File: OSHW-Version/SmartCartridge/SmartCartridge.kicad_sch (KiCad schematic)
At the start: 9 parts

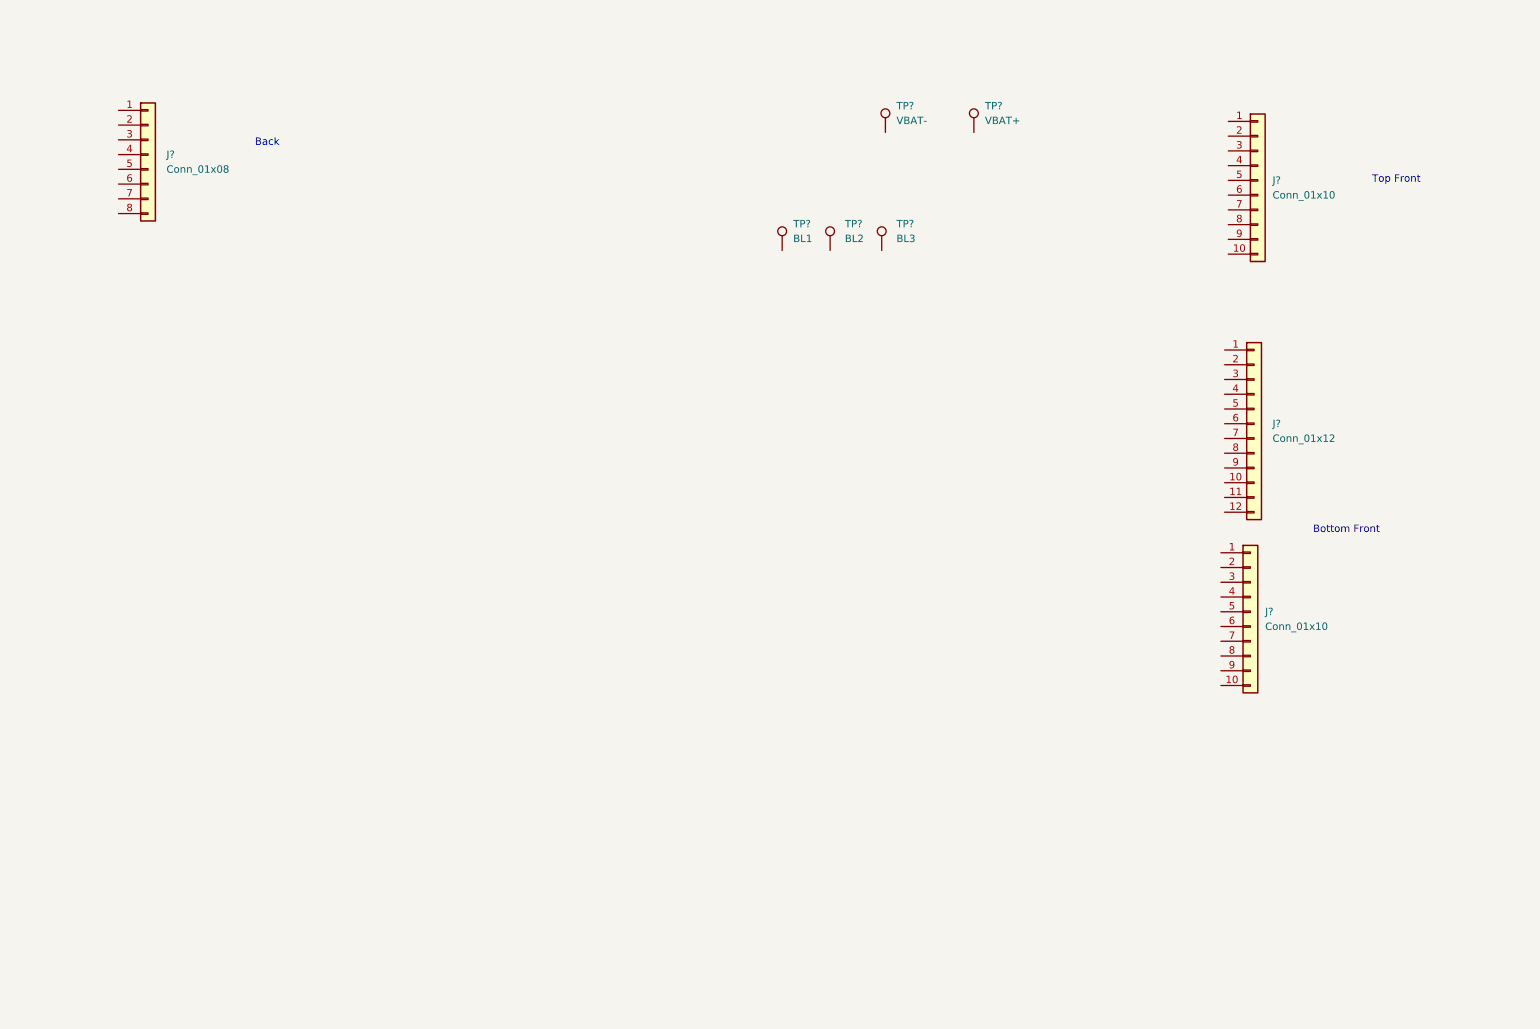
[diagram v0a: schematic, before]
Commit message: SmartCartridge Kicad : brushless, battery connector and button placement
+ spotted all the ground
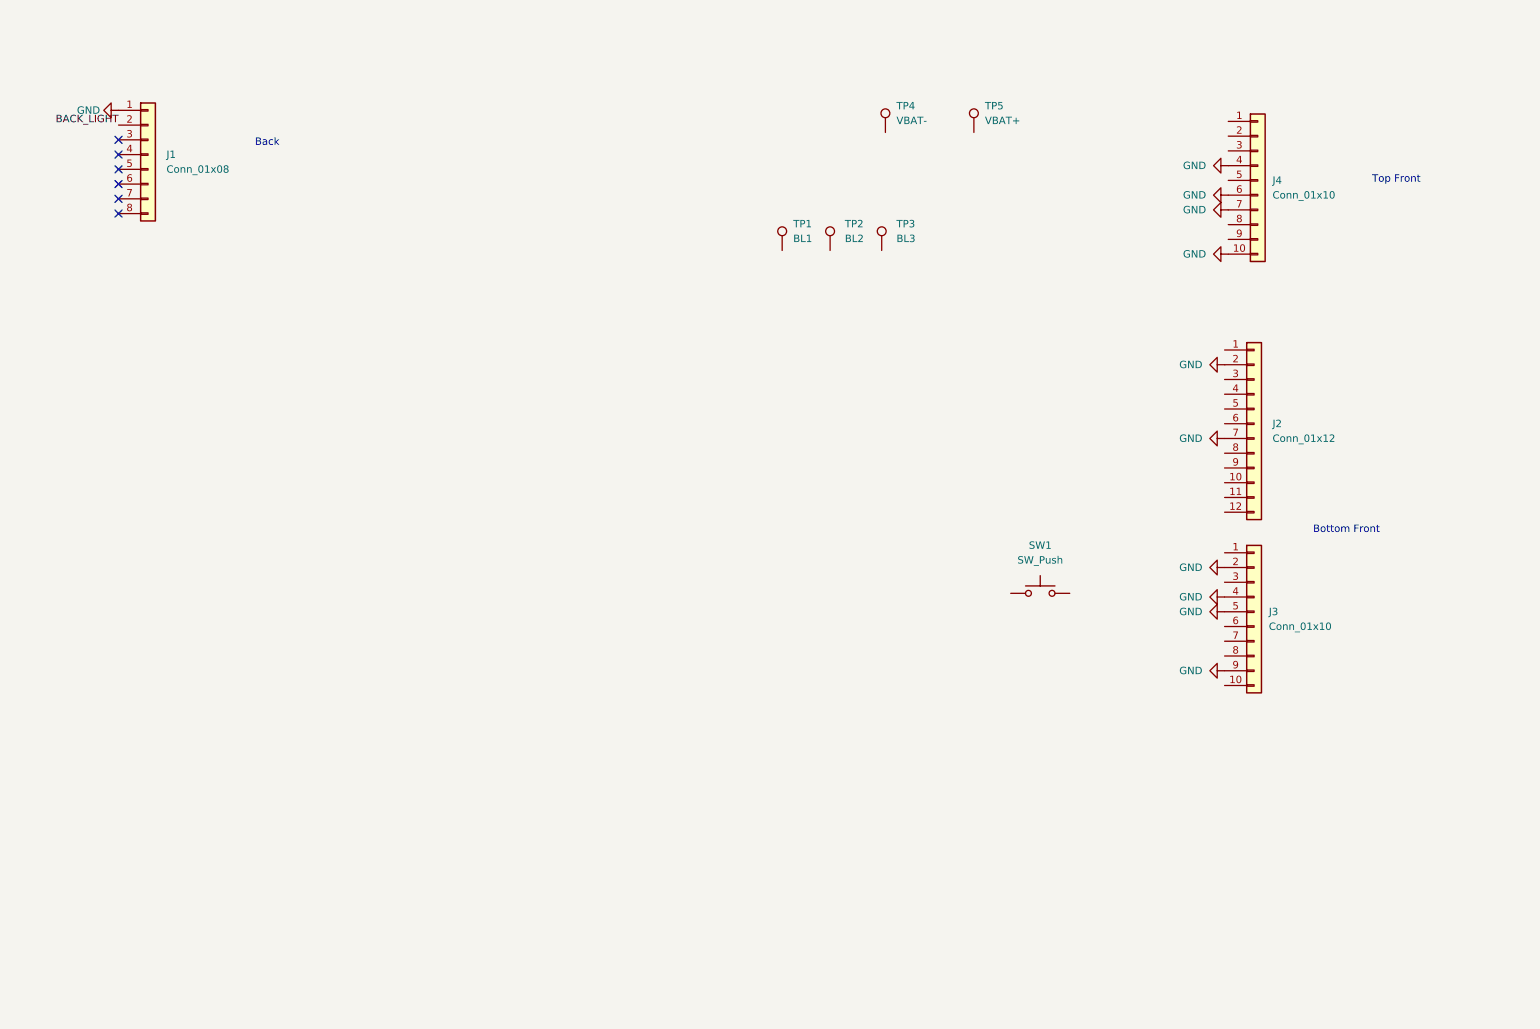
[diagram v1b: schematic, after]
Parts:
- added SW1: SW_Push, Button_Switch_THT:SW_PUSH_6mm, symbol Switch:SW_Push
- TP1, TP2, TP3, TP4, TP5: renamed from TP?; footprint (none) -> TestPoint:TestPoint_Loop_D3.80mm_Drill2.5mm
- gave numbers to parts that had none: 4
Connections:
- net GND: now reaches J3.2 (Pin_2)
- net GND: now also J1.1 (Pin_1), J2.2 (Pin_2), J2.7 (Pin_7), J3.4 (Pin_4), J3.5 (Pin_5), J3.9 (Pin_9), J4.10 (Pin_10), J4.4 (Pin_4), J4.6 (Pin_6), J4.7 (Pin_7)
- net BACK_LIGHT: now reaches J1.2 (Pin_2)
- no-connect marks 0 -> 6
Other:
- moved on the sheet: J3

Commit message: readme refacto, add datasheet, add led display, progress smartcartridge
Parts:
- added H1, H2, H3, H4, H5, H6: MountingHole, MountingHole:MountingHole_2.2mm_M2, symbol Mechanical:MountingHole
- added J5: USB_C_Receptacle, Connector_USB:USB_C_Receptacle_JAE_DX07S024WJ1R350, symbol Connector:USB_C_Receptacle
- added U1: ProS3, footprint:ProS3_TH, symbol ProS3:ProS3
- added U2: TXB0108DQSR, Package_SON:USON-20_2x4mm_P0.4mm, symbol Logic_LevelTranslator:TXB0108DQSR
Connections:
- net GND: now also J4.3 (Pin_3); no longer J4.7 (Pin_7)
- new net: J5.A1 (GND), J5.A12 (GND), J5.B1 (GND), J5.B12 (GND)
- new net: J5.A4 (VBUS), J5.A9 (VBUS), J5.B4 (VBUS), J5.B9 (VBUS)
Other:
- note added: "2 pin (or less) for front light"
- note added: "4 pin (or less) for battery"
- note added: "4 pin (or less) for e shifter"
- note added: "4 pin (or less) for kick lock"
- note added: "C22"
- note added: "R84 - Q29 - R83 - Q30"
- note added: "TP196"
- note added: "Targeting USB PD 3.1 36V@5A"
